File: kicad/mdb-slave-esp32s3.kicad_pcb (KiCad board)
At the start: 2 copper layers, 39 x 41 mm, 35 parts, among them J1 MDB_Connector, J2 USB_C_Receptacle_USB2.0_16P, J3 Conn_02x11_Odd_Even, SW1 SW_Push, U1 TLP785, U2 KA78M05_TO252, U3 ESP32-S3FH4R2, U4 TLP785, Y1 Crystal_GND24

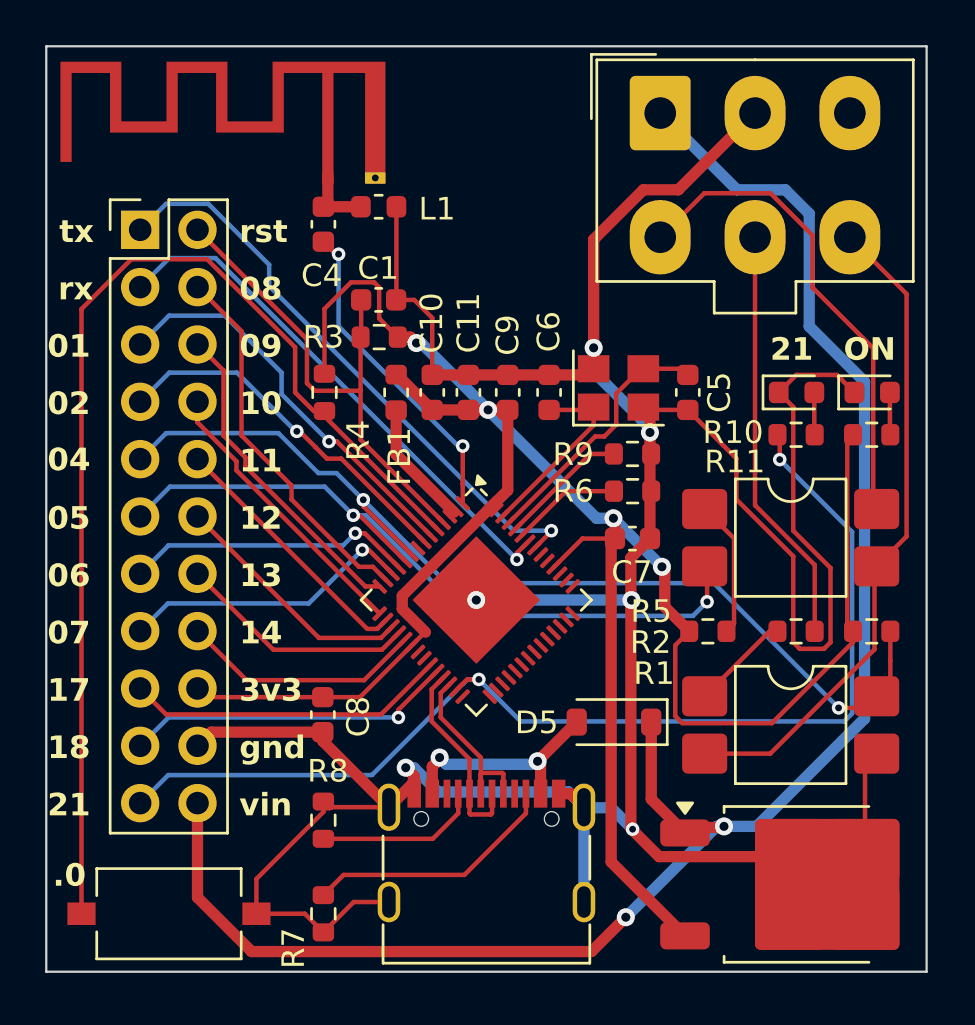
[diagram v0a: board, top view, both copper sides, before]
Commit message: Migrate from LDO regulator to conversor buck
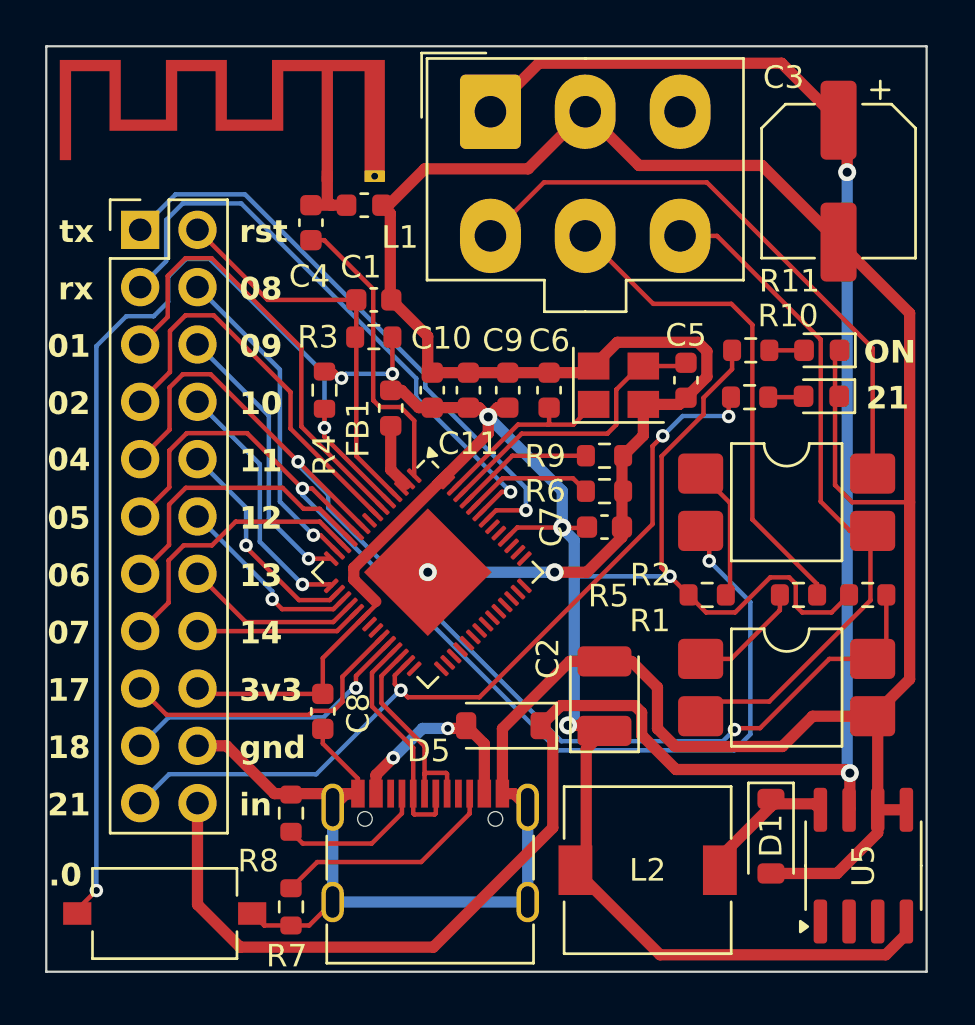
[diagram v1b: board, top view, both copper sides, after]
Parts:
- removed U2: KA78M05_TO252, Package_TO_SOT_SMD:TO-252-2
- added C2: 220uF, Capacitor_Tantalum_SMD:CP_EIA-3528-21_Kemet-B, F.Cu at (193.2, 111.9)
- added C3: 100uF, Capacitor_SMD:CP_Elec_6.3x5.8, F.Cu at (203.6, 89.1)
- added D1: D_Schottky, Diode_SMD:D_SOD-123, F.Cu at (200.6, 118.1)
- added L2: 100uH, Inductor_SMD:L_7.3x7.3_H3.5, F.Cu at (195.1, 119.6)
- added REF**: OSHW-Logo2_9.8x8mm_SilkScreen, Symbol:OSHW-Logo2_9.8x8mm_SilkScreen, B.Cu at (181.7, 93.4)
- added U5: LM2594HVM-3.3, Package_SO:SOIC-8_3.9x4.9mm_P1.27mm, F.Cu at (204.7, 119.4)
- moved J1 7.52 mm to (188.2, 86.0)
- moved R11 6.54 mm to (199.7, 96.6)
- moved D5 4.90 mm to (188.8, 113.2)
- moved D3 2.91 mm to (202.9, 96.6), turned to 180 degrees
- moved R10 2.65 mm to (199.7, 98.6)
- moved J2 2.49 mm to (185.5, 119.9)
- moved U3 2.48 mm to (185.4, 106.4)
- moved U4 1.67 mm to (201.3, 111.5)
- moved R1 1.62 mm to (204.9, 107.4)
- moved R2 1.62 mm to (201.8, 107.4)
- moved R5 1.61 mm to (197.8, 107.4)
- moved U1 1.58 mm to (201.3, 103.3)
- moved R8 1.47 mm to (179.3, 117.1)
- moved R7 1.46 mm to (179.3, 121.2)
- moved C7 1.34 mm to (193.2, 104.4)
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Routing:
- net /io5: track 33.0 -> 48.9 mm
- net GND: track 154.6 -> 169.5 mm, vias 6 -> 2
- net /vin: track 78.2 -> 92.0 mm
- net /io21: track 49.6 -> 37.9 mm, vias 2 -> 3
- net Net-(D1-K): track 0.00 -> 6.48 mm
- net /io4: track 44.8 -> 50.9 mm
- net /reset: track 22.7 -> 17.7 mm
- net /mdb_master_receive: track 21.6 -> 26.5 mm
- net /mdb_master_transmit: track 18.6 -> 22.2 mm
- net /io14: track 10.9 -> 7.42 mm
- net /u0rxd: track 23.7 -> 26.6 mm
- net VDD3P3: track 5.58 -> 2.86 mm
- net /io13: track 10.6 -> 7.97 mm
- net /io12: track 11.1 -> 8.60 mm, vias 0 -> 1
- net /io8: track 16.8 -> 14.5 mm, vias 0 -> 1
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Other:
- board text added: "in"
- board text added: "vmflow.xyz"
- board text removed: "mdb-target-esp32s3"
- board text removed: "vin"

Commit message: Adding buzzer and ws2812b LED Addressable
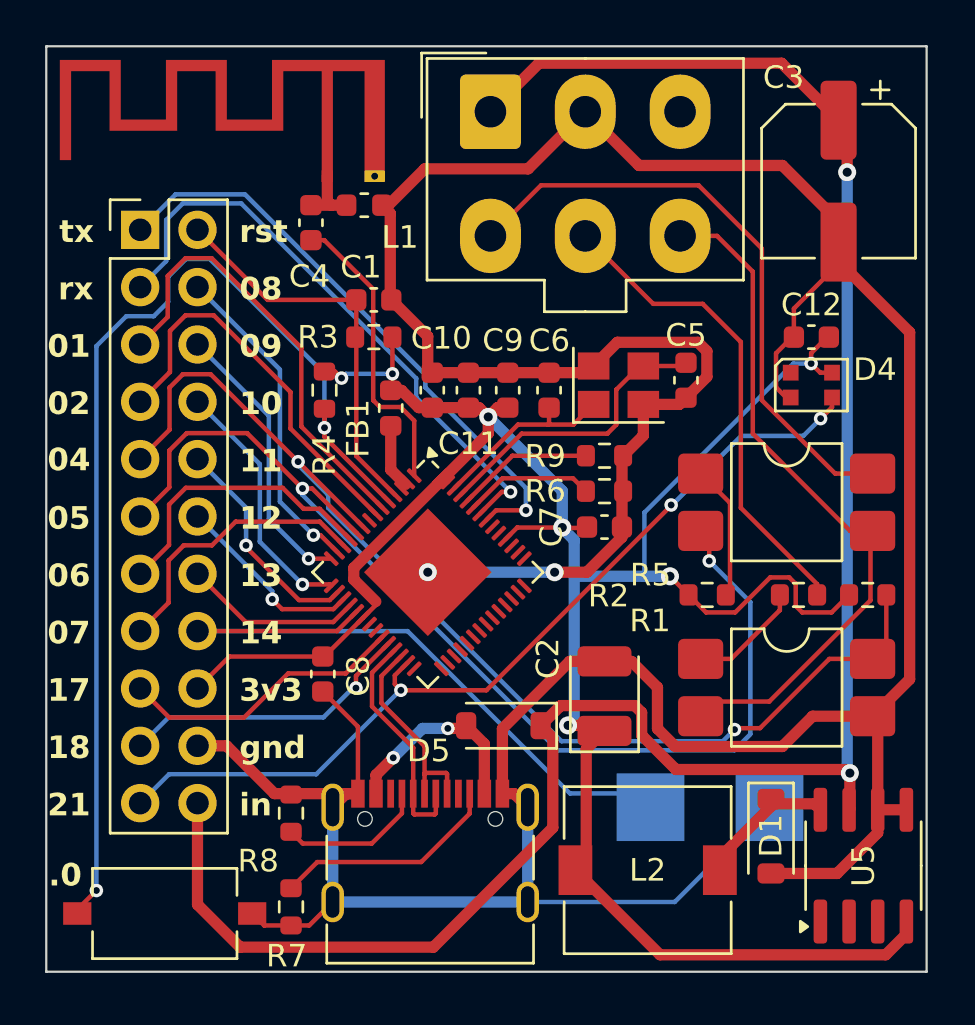
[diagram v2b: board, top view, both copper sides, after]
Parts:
- removed D2, D3: LED, LED_SMD:LED_0603_1608Metric
- removed R10, R11: 1k, Resistor_SMD:R_0603_1608Metric
- removed the REF** at (181.7, 93.4)
- added C12: 0.1uF, Capacitor_SMD:C_0603_1608Metric, F.Cu at (202.4, 96.0)
- added D4: WS2812B-2020, LED_SMD:LED_WS2812B-2020_PLCC4_2.0x2.0mm, F.Cu at (202.4, 98.1)
- added REF**: OSHW-Logo2_14.6x12mm_SilkScreen, Symbol:OSHW-Logo2_14.6x12mm_SilkScreen, B.Cu at (188.0, 103.6)
- added gnd: Buzzer_Flag (-), TestPoint:TestPoint_Pad_3.0x3.0mm, B.Cu at (200.5, 116.8)
- added io14: Buzzer_Flag (14), TestPoint:TestPoint_Pad_3.0x3.0mm, B.Cu at (195.3, 116.8)
- moved C8 1.66 mm to (180.8, 110.9)
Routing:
- net /io14: track 7.42 -> 30.7 mm
- net GND: track 169.5 -> 182.8 mm
- net +3V3: track 104.9 -> 108.2 mm, vias 6 -> 7
- net /io21: track 37.9 -> 39.9 mm
- net Net-(D2-A): track 1.64 -> 0.00 mm
- net Net-(D3-A): track 1.54 -> 0.00 mm
- net /mdb_master_transmit: track 22.2 -> 21.4 mm
- net /mdb_master_receive: track 26.5 -> 27.1 mm
- net /io17: track 13.3 -> 12.7 mm
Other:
- board text added: "Buzzer..."
- board text added: "VMflow.xyz"
- board text added: "mdb-target-esp32s3"
- board text removed: "ON"
- board text removed: "vmflow.xyz"

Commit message: XINGLIGHT XL-2121RGBC-2812B LED Addressable
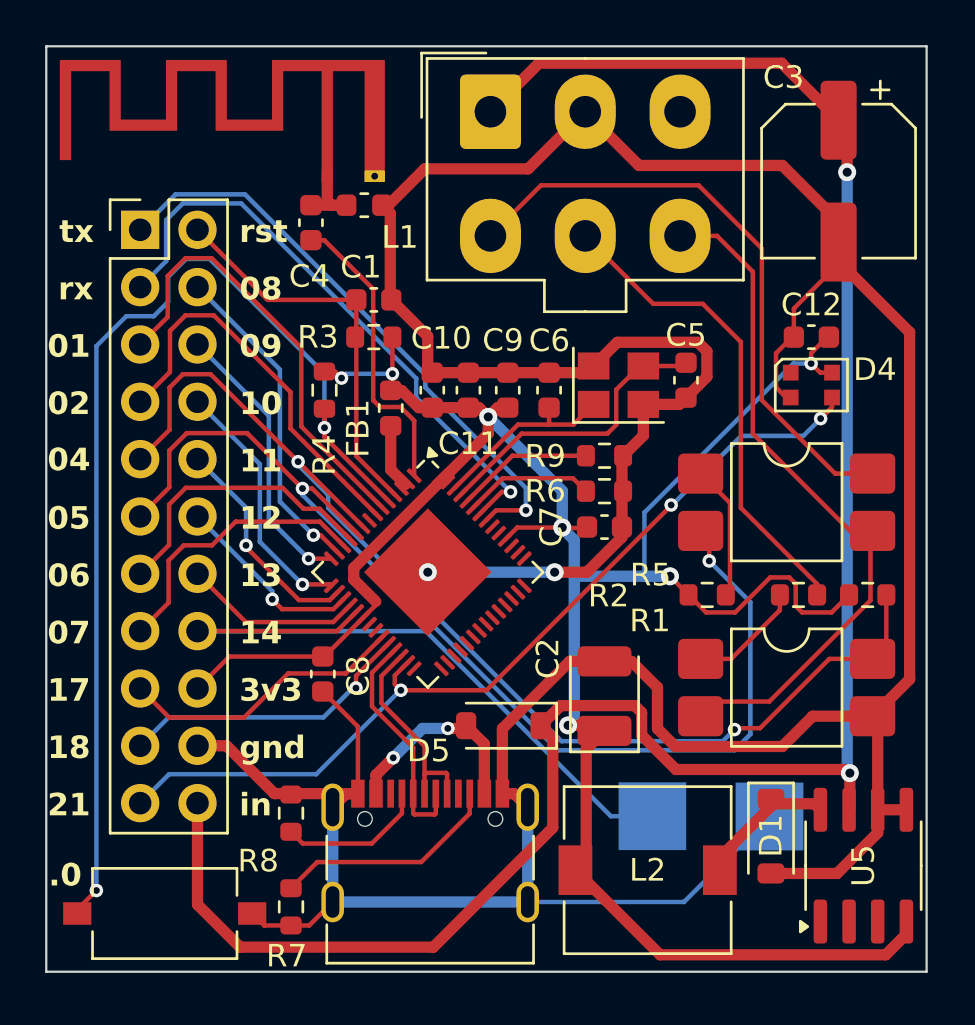
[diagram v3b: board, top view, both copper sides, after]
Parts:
- removed gnd: Buzzer_Flag (-), TestPoint:TestPoint_Pad_3.0x3.0mm
- removed io14: Buzzer_Flag (14), TestPoint:TestPoint_Pad_3.0x3.0mm
- added TP1: Buzzer_Flag (14), TestPoint:TestPoint_Pad_3.0x3.0mm, B.Cu at (195.3, 117.2)
- added TP2: Buzzer_Flag (-), TestPoint:TestPoint_Pad_3.0x3.0mm, B.Cu at (200.5, 117.2)
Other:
- board text added: "io14"

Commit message: Aligning components
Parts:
- TP1, TP2: footprint TestPoint:TestPoint_Pad_3.0x3.0mm -> TestPoint:TestPoint_Pad_2.0x2.0mm
- moved TP1 1.38 mm to (196.6, 116.6)
- moved TP2 0.63 mm to (200.5, 116.6)
- moved C12 0.52 mm to (201.9, 96.0)
- moved D4 0.26 mm to (202.1, 98.1)
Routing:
- net /io14: track 31.0 -> 31.9 mm

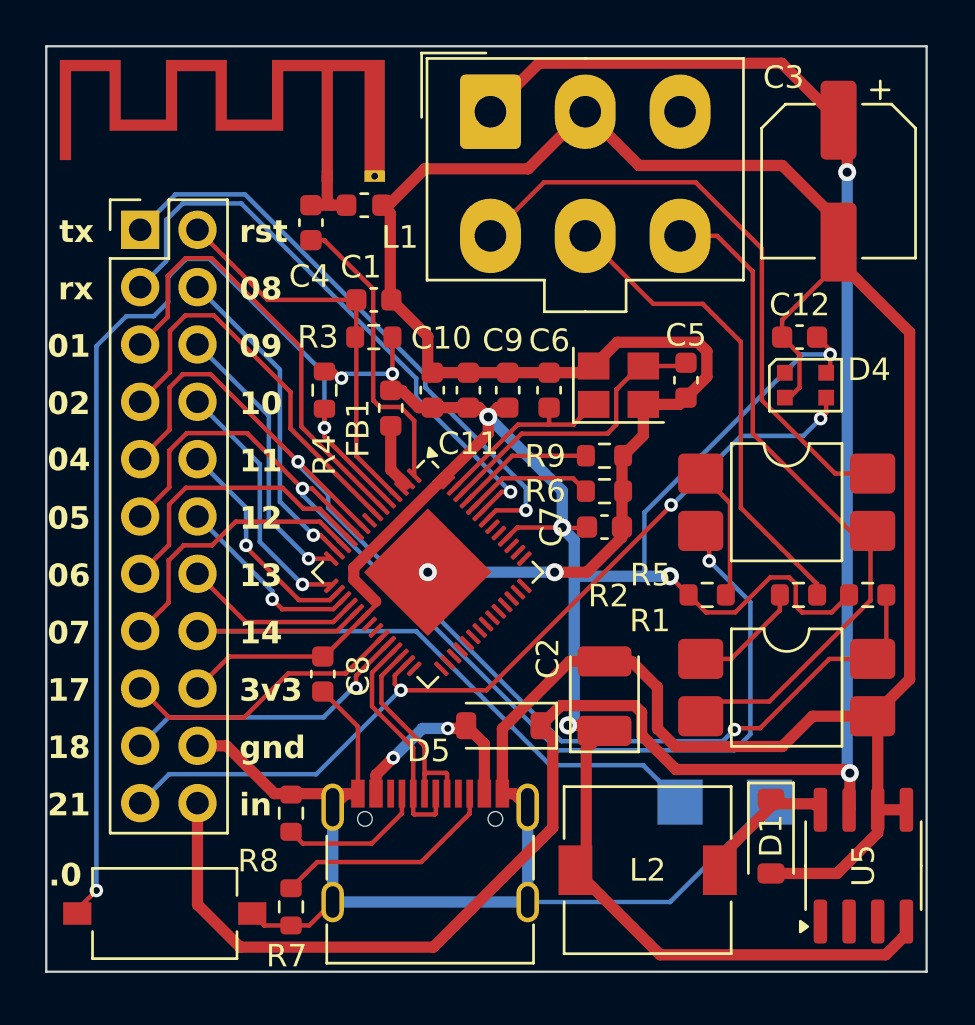
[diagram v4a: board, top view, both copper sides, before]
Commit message: bug fixing - Changing 10k resistor -> 1k resistor
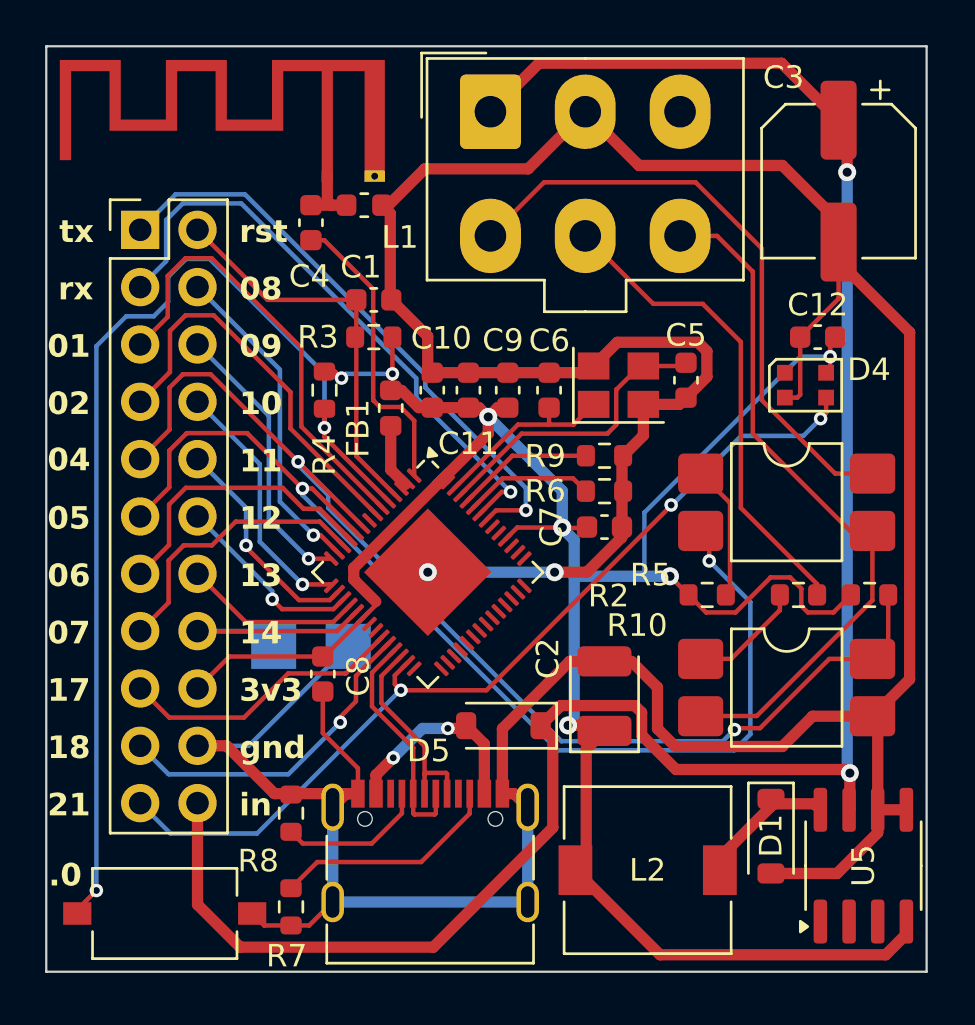
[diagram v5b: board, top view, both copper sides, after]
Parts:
- removed R1: 10K, Resistor_SMD:R_0603_1608Metric
- added R10: 1k, Resistor_SMD:R_0603_1608Metric, F.Cu at (205.0, 107.4)
- moved TP2 19.9 mm to (181.9, 109.7)
- moved TP1 19.3 mm to (178.6, 109.7)
- moved REF** 4.50 mm to (192.4, 104.5)
- moved C12 0.80 mm to (202.7, 96.0)
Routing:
- net /io14: track 31.9 -> 11.1 mm
- net GND: track 182.8 -> 178.6 mm
- net /io18: track 13.2 -> 14.7 mm
- net /io21: track 39.8 -> 40.9 mm
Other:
- board text removed: "Buzzer..."
